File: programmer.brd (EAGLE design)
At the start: 50.8 x 25.4 mm, 16 parts, among them U1 ATMEGA8U2AU, Y1 16 MHz

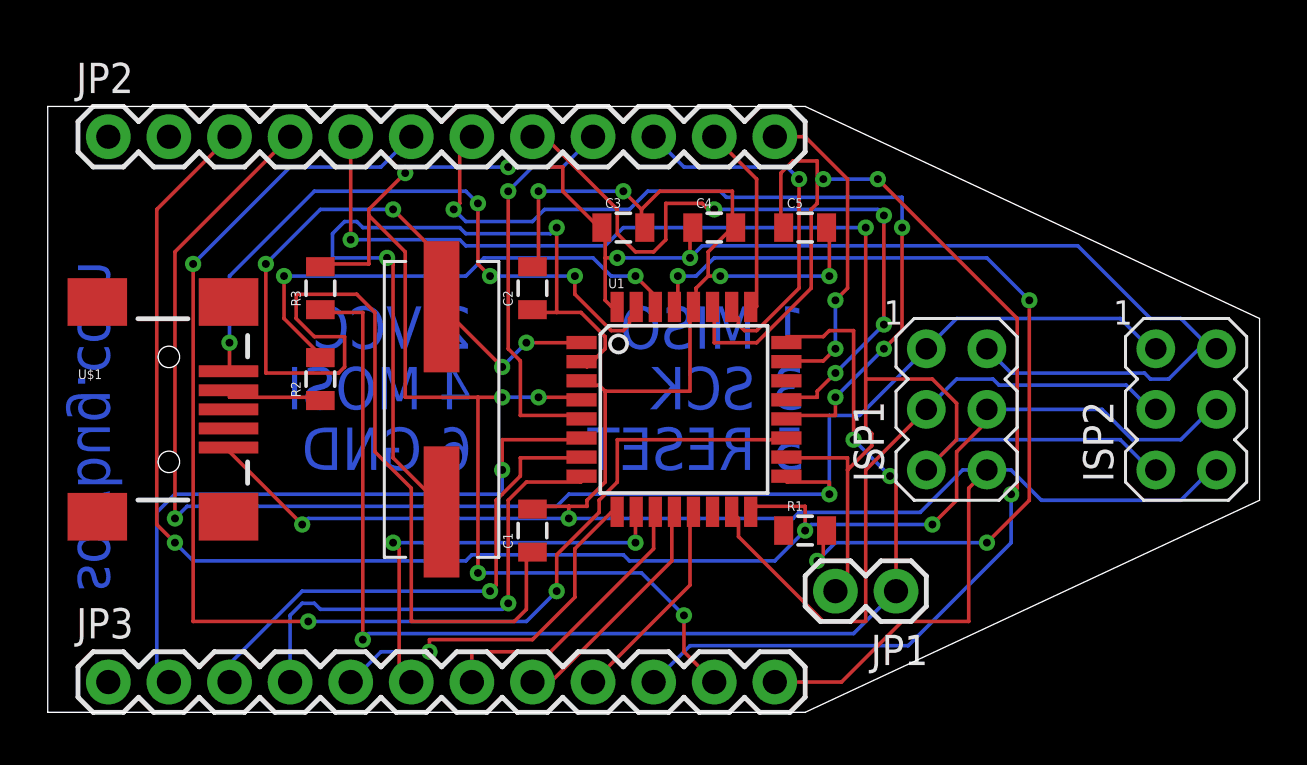
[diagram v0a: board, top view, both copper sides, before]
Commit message: Angled 6-pin ISP.
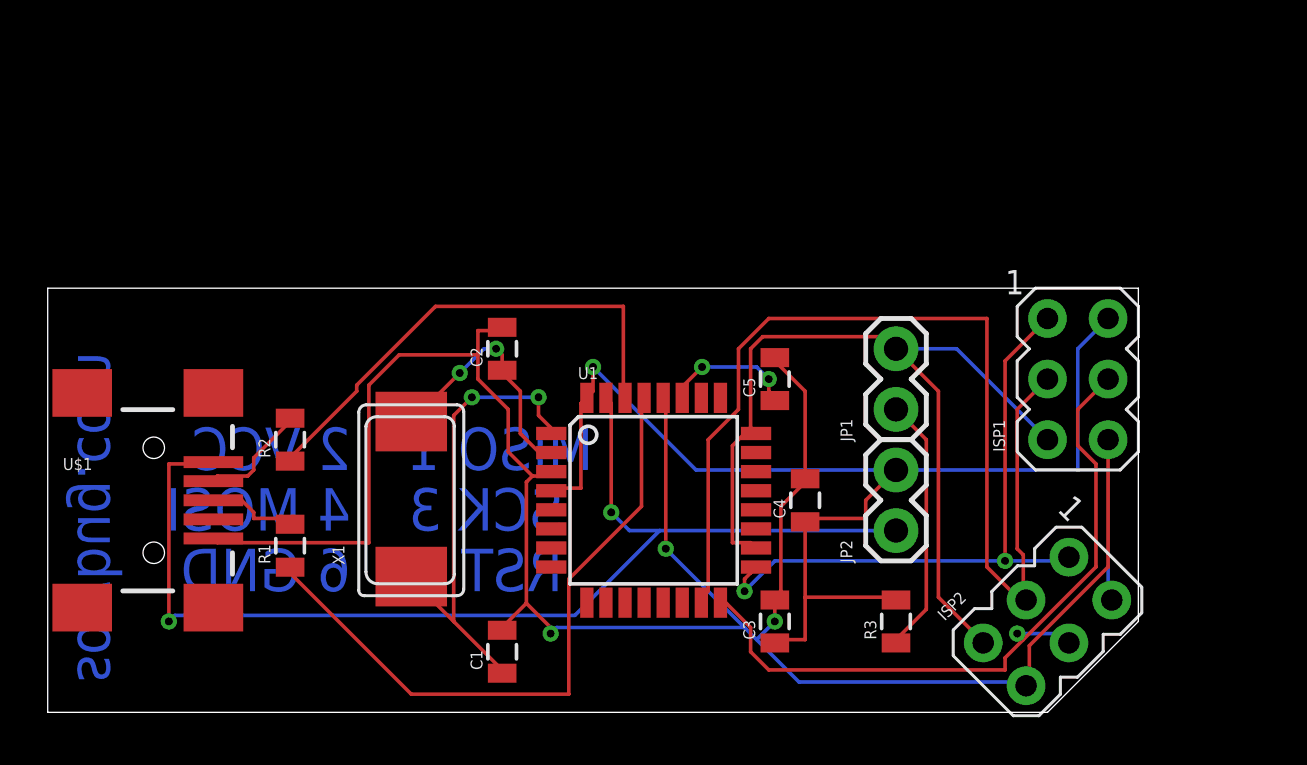
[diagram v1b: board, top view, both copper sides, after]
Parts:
- removed JP3: M12PTH, SparkFun:1X12
- removed Y1: 16 MHz, SparkFun:CRYSTAL-SMD-10.5X4.8-2PIN
- added X1: 16MHz, adafruit:NX8045
- JP2: value M12PTH -> VCC; device SparkFun:1X12 -> SparkFun:1X02
- moved JP2 36.9 mm to (35.6, 7.62), turned to 90 degrees
- moved R3 27.9 mm to (35.6, 3.81)
- moved R1 21.6 mm to (10.2, 6.99), turned to 90 degrees
- moved C3 17.7 mm to (30.5, 3.81), turned to 90 degrees
- moved C4 12.0 mm to (31.8, 8.89), turned to 90 degrees
- moved ISP2 10.6 mm to (41.9, 3.81), turned to 315 degrees
- moved JP1 7.62 mm to (35.6, 12.7), turned to 90 degrees
- moved C5 6.48 mm to (30.5, 14.0), turned to 90 degrees
- moved C1 5.24 mm to (19.1, 2.54)
- moved ISP1 5.24 mm to (43.2, 14.0)
- moved U1 4.02 mm to (25.4, 8.89)
- moved U$1 3.86 mm to (4.45, 8.89)
- moved C2 2.84 mm to (19.1, 15.2)
- moved R2 2.84 mm to (10.2, 11.4)
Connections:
- removed net D_MINUS: R2.1, U$1.D-
- removed net D_MINUS_MCU: R2.2, U1.30
- removed net D_PLUS: R1.1, U$1.D+
- removed net D_PLUS_MCU: R1.2, U1.29
- removed net N$5: U$1.VBUS, U1.31
- removed net PB0: JP2.1, U1.14
- removed net PB1: ISP1.3, ISP2.3, JP2.2, U1.15
- removed net PB2: ISP1.4, ISP2.4, JP2.3, U1.16
- removed net PB3: ISP1.1, ISP2.1, JP2.4, U1.17
- removed net PB4: ISP1.5, ISP2.5, JP1.2, JP2.5, U1.18
- removed net PB5: JP2.6, U1.19
- removed net PB6: JP2.7, U1.20
- removed net PB7: JP2.8, U1.21
- removed net PC2: JP2.9, U1.5
- removed net PC4: JP2.10, U1.26
- removed net PC5: JP2.11, U1.25
- removed net PC6: JP2.12, U1.23
- removed net PC7: JP3.1, U1.22
- removed net PD0: JP3.2, U1.6
- removed net PD1: JP3.3, U1.7
- removed net PD2: JP3.4, U1.8
- removed net PD3: JP3.5, U1.9
- removed net PD4: JP3.6, U1.10
- removed net PD5: JP3.7, U1.11
- removed net PD6: JP3.8, U1.12
- removed net PD7: JP3.9, U1.13
- new net 5V: JP2.1, U$1.VBUS, U1.31
- new net D+: R1.1, U1.29
- new net D+RAW: R1.2, U$1.D+
- new net D-: R2.1, U1.30
- new net MISO: ISP1.1, ISP2.1, U1.17
- new net MOSI: ISP1.4, ISP2.4, U1.16
- new net N$2: R2.2, U$1.D-
- new net RST: ISP1.5, ISP2.5, JP1.2, U1.18, U1.24
- new net SCK: ISP1.3, ISP2.3, U1.15
- net 3.3V: no longer JP3.10
- net GND: no longer JP3.12
- net RST_JP1: no longer U1.24
- net VCC: now also JP2.2; no longer JP3.11
- net XTAL1: now also X1.P$2; no longer Y1.P$2
- net XTAL2: now also X1.P$1; no longer Y1.P$1
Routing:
- net PB2: track 71.3 -> 0.00 mm, vias 3 -> 0
- net PB3: track 67.6 -> 0.00 mm, vias 2 -> 0
- net PB4: track 63.6 -> 0.00 mm, vias 2 -> 0
- net PB5: track 56.6 -> 0.00 mm, vias 3 -> 0
- net 3.3V: track 53.8 -> 5.67 mm, vias 3 -> 2
- net 5V: track 0.00 -> 47.8 mm, vias 0 -> 2
- net SCK: track 0.00 -> 44.9 mm
- net RST_JP1: track 53.6 -> 10.8 mm, vias 3 -> 0
- net RST: track 0.00 -> 38.4 mm
- net VCC: track 96.0 -> 57.9 mm, vias 8 -> 1
- net D_PLUS_MCU: track 37.0 -> 0.00 mm, vias 4 -> 0
- net XTAL1: track 55.9 -> 19.9 mm, vias 4 -> 2
- net PB6: track 35.5 -> 0.00 mm, vias 4 -> 0
- net MOSI: track 0.00 -> 31.0 mm, vias 0 -> 1
- net PB7: track 29.4 -> 0.00 mm, vias 4 -> 0
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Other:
- board size 50.8 x 25.4 mm -> 45.7 x 17.8 mm
- board text added: "MISO 1"
- board text added: "RST 5"
- board text added: "SCK 3"
- board text removed: "1 MISO"
- board text removed: "3 SCK"
- board text removed: "5 RESET"

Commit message: Blinkenlights.
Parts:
- added LED1, LED2: (no value), adafruit:1206
- added R4, R5: 1K, SparkFun:0805
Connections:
- new net LED_ACTIVE: LED2.C, U1.7
- new net LED_WRITE: LED1.C, U1.6
- new net N$1: LED2.A, R5.1
- new net N$3: LED1.A, R4.1
- net VCC: now also R4.2, R5.2
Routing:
- net VCC: track 57.9 -> 92.9 mm, vias 1 -> 3
- net LED_WRITE: track 0.00 -> 29.5 mm
- net SCK: track 44.9 -> 29.4 mm
- net LED_ACTIVE: track 0.00 -> 15.0 mm, vias 0 -> 2
- net XTAL1: track 19.9 -> 31.4 mm, vias 2 -> 0
- net MOSI: track 31.0 -> 42.5 mm
- net N$3: track 0.00 -> 6.57 mm
- net N$1: track 0.00 -> 6.57 mm
- net D+: track 27.7 -> 23.7 mm, vias 0 -> 2
- net GND: track 93.1 -> 89.3 mm, vias 3 -> 5
- net RST: track 38.4 -> 39.7 mm
- net D-: track 20.8 -> 19.5 mm, vias 0 -> 2
- net 5V: track 47.8 -> 48.7 mm
- net XTAL2: track 10.4 -> 10.9 mm
- net MISO: track 26.3 -> 26.7 mm, vias 2 -> 1

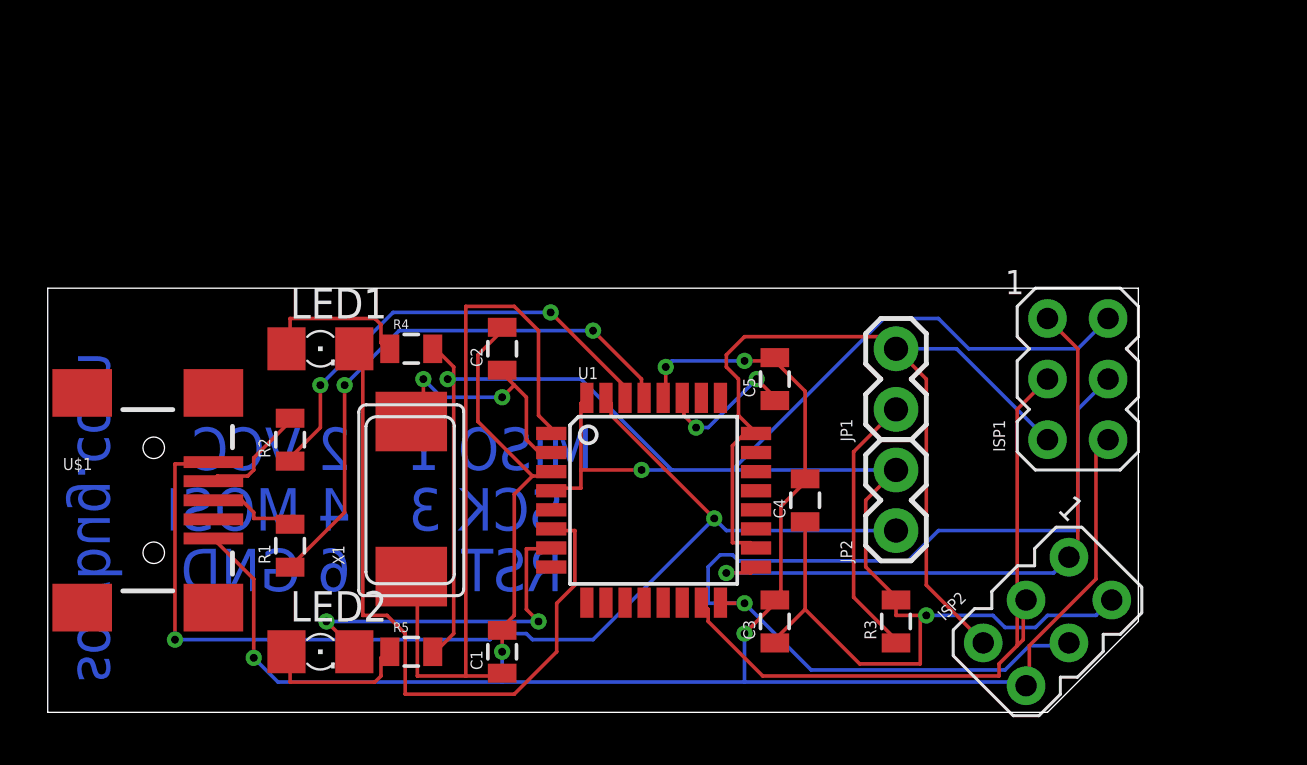
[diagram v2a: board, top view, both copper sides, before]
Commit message: More work on layout. SJ1. Polarized 10uF cap. Fixed ISP2 orientation.
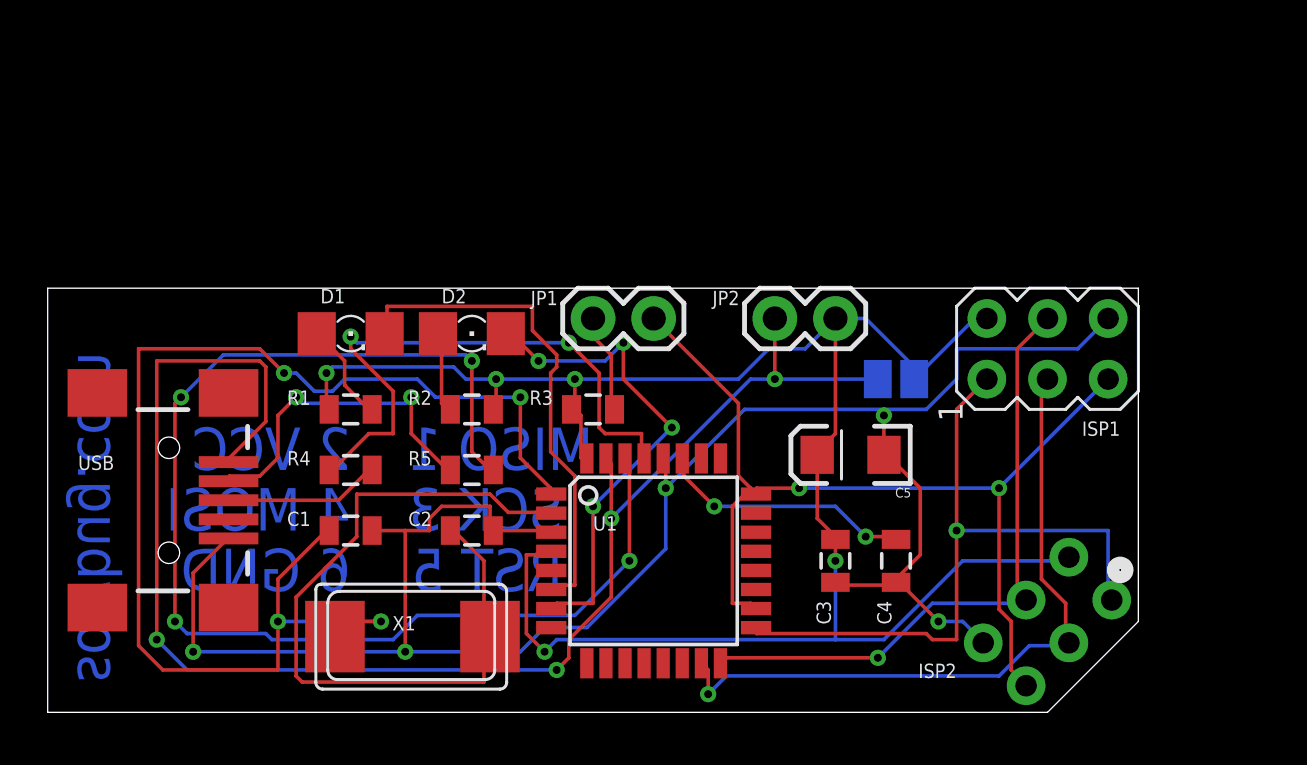
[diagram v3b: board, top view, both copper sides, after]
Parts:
- removed LED1, LED2: (no value), adafruit:1206
- removed U$1: USB-MINIB-5PIN, SparkFun:USB-MINIB
- added D1: WRITE, adafruit:1206
- added D2: ACTIVITY, adafruit:1206
- added SJ1: VCC-5V, jumper:SJ
- added USB: USB-MINIB-5PIN, SparkFun:USB-MINIB
- C4: value 10 uF -> 0.1 uF
- C5: value 0.1 uF -> 10 uF; device SparkFun:0805 -> SparkFun:EIA3216
- JP1: value SELFPGM -> SELF-PGM
- JP2: value VCC -> VCC-5V
- R1, R2: value 22 -> 1K
- R4, R5: value 1K -> 22
- moved R3 15.5 mm to (22.9, 12.7), turned to 0 degrees
- moved JP1 13.3 mm to (22.9, 16.5), turned to 0 degrees
- moved JP2 10.2 mm to (30.5, 16.5), turned to 0 degrees
- moved C1 8.13 mm to (12.7, 7.62), turned to 0 degrees
- moved R5 8.03 mm to (17.8, 10.2)
- moved R2 7.73 mm to (17.8, 12.7), turned to 0 degrees
- moved C2 7.73 mm to (17.8, 7.62), turned to 0 degrees
- moved R1 6.25 mm to (12.7, 12.7), turned to 0 degrees
- moved X1 5.72 mm to (15.2, 3.17), turned to 0 degrees
- moved R4 5.68 mm to (12.7, 10.2)
- moved C4 4.58 mm to (35.6, 6.35)
- moved C5 4.49 mm to (33.7, 10.8), turned to 180 degrees
- moved C3 3.59 mm to (33.0, 6.35)
- moved U1 2.54 mm to (25.4, 6.35)
- moved ISP1 1.80 mm to (41.9, 15.2), turned to 90 degrees
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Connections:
- net 3.3V: now also C4.2; no longer C5.1
- net 5V: now also SJ1.2, USB.VBUS; no longer U$1.VBUS
- net D+: now also R4.1; no longer R1.1
- net D+RAW: now also R4.2, USB.D+; no longer R1.2, U$1.D+
- net D-: now also R5.2; no longer R2.1
- net GND: now also C3.1, C4.1, C5.C, USB.GND; no longer C3.2, C4.2, C5.2, U$1.GND
- net LED_ACTIVE: now also D2.C; no longer LED2.C
- net LED_WRITE: now also D1.C; no longer LED1.C
- net N$1: now also D2.A, R2.1; no longer LED2.A, R5.1
- net N$2: now also R5.1, USB.D-; no longer R2.2, U$1.D-
- net N$3: now also D1.A, R1.2; no longer LED1.A, R4.1
- net RST_JP1: now also R3.2; no longer R3.1
- net VCC: now also C3.2, C5.A, R1.1, R2.2, R3.1, SJ1.1; no longer C3.1, C4.1, R3.2, R4.2, R5.2
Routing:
- net D-: track 19.5 -> 52.7 mm, vias 2 -> 4
- net XTAL1: track 31.4 -> 54.2 mm, vias 0 -> 4
- net XTAL2: track 10.9 -> 32.5 mm, vias 2 -> 0
- net MOSI: track 42.5 -> 26.4 mm
- net 5V: track 48.7 -> 64.3 mm, vias 2 -> 4
- net VCC: track 92.9 -> 81.4 mm, vias 3 -> 5
- net N$2: track 4.70 -> 14.3 mm, vias 0 -> 2
- net LED_WRITE: track 29.5 -> 21.0 mm
- net RST_JP1: track 11.3 -> 4.26 mm
- net GND: track 89.3 -> 83.5 mm
- net LED_ACTIVE: track 15.0 -> 20.8 mm, vias 2 -> 4
- net 3.3V: track 6.06 -> 10.8 mm
- net N$1: track 6.57 -> 3.47 mm
- net MISO: track 26.7 -> 29.5 mm
- net D+RAW: track 3.92 -> 6.55 mm
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
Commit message: Wider. Added SJ1 connection.
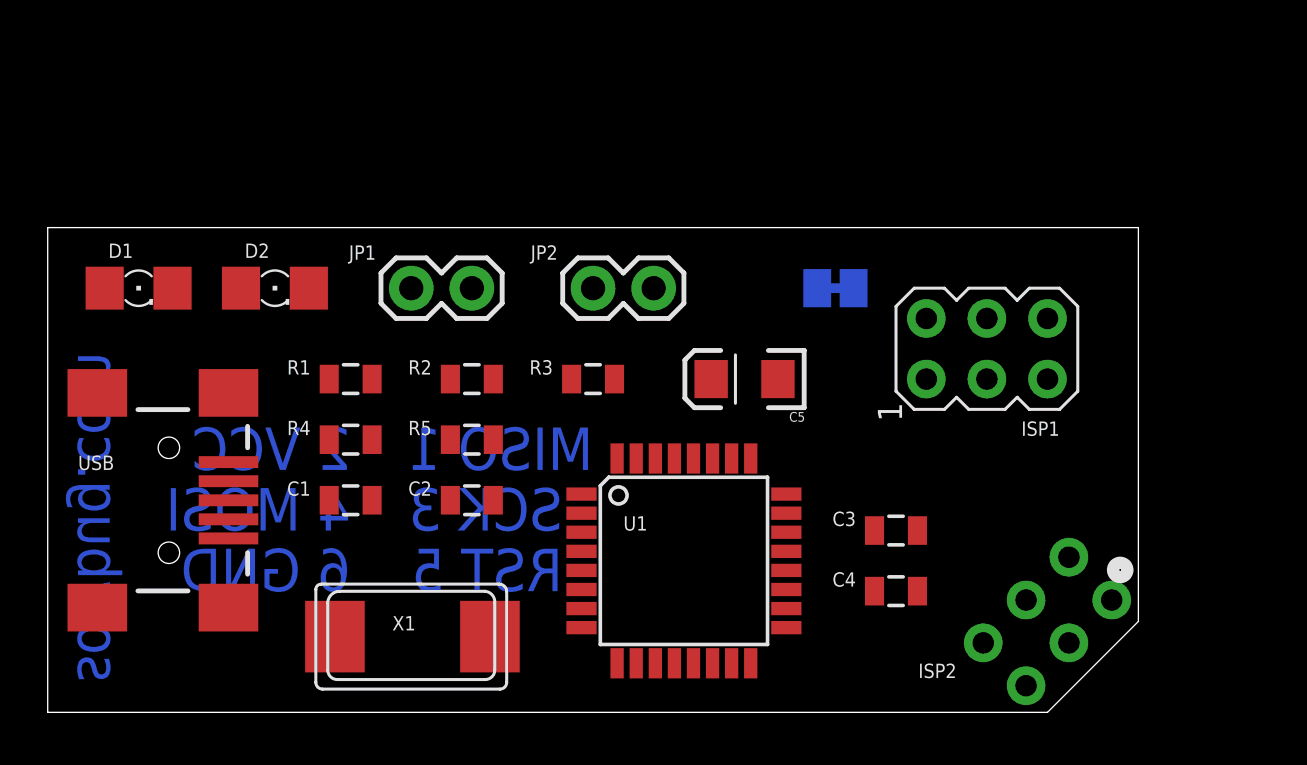
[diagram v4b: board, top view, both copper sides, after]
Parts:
- moved D1 9.09 mm to (3.81, 17.8)
- moved D2 8.47 mm to (9.53, 17.8)
- moved JP2 7.73 mm to (22.9, 17.8)
- moved JP1 7.73 mm to (15.2, 17.8)
- moved C5 5.46 mm to (29.2, 14.0)
- moved SJ1 4.58 mm to (33.0, 17.8)
- moved C3 2.84 mm to (35.6, 7.62), turned to 0 degrees
- moved ISP1 2.54 mm to (39.4, 15.2)
- moved U1 1.27 mm to (26.7, 6.35)
- moved R1 1.27 mm to (12.7, 14.0)
- moved R2 1.27 mm to (17.8, 14.0)
- moved R3 1.27 mm to (22.9, 14.0)
- moved C1 1.27 mm to (12.7, 8.89)
- moved C2 1.27 mm to (17.8, 8.89)
- moved C4 1.27 mm to (35.6, 5.08), turned to 0 degrees
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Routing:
- net GND: track 83.5 -> 0.00 mm, vias 5 -> 0
- net VCC: track 81.4 -> 0.00 mm, vias 5 -> 0
- net 5V: track 64.3 -> 0.00 mm, vias 4 -> 0
- net XTAL1: track 54.2 -> 0.00 mm, vias 4 -> 0
- net D-: track 52.7 -> 0.00 mm, vias 4 -> 0
- net RST: track 41.0 -> 0.00 mm, vias 2 -> 0
- net XTAL2: track 32.5 -> 0.00 mm
- net MISO: track 29.5 -> 0.00 mm, vias 1 -> 0
- net SCK: track 29.1 -> 0.00 mm, vias 1 -> 0
- net MOSI: track 26.4 -> 0.00 mm, vias 1 -> 0
- net D+: track 24.5 -> 0.00 mm, vias 2 -> 0
- net LED_WRITE: track 21.0 -> 0.00 mm
- net LED_ACTIVE: track 20.8 -> 0.00 mm, vias 4 -> 0
- net N$2: track 14.3 -> 0.00 mm, vias 2 -> 0
- net 3.3V: track 10.8 -> 0.00 mm, vias 2 -> 0
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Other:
- board size 45.7 x 17.8 mm -> 45.7 x 20.3 mm
